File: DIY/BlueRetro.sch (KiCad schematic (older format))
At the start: 22 parts, among them J2 Conn_01x19, J3 Conn_01x19, P1 DC Ctrl slot, P1 GC Ctrl slot, P1 N64 Ctrl slot, P2 DC Ctrl slot, P2 GC Ctrl slot, P2 N64 Ctrl slot, P3 DC Ctrl slot, P3 GC Ctrl slot, P3 N64 Ctrl slot, P4 DC Ctrl slot, P4 GC Ctrl slot, P4 N64 Ctrl slot

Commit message: [DIY] Update DIY & cable adapter schematic base on new DB25 mapping
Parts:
- removed J?: DB25_Female, symbol Connector:DB25_Female
- removed J? (x3): DB25_Male, symbol Connector:DB25_Male
- removed JP1, JP2: Conn_02x14_Odd_Even, symbol Connector_Generic:Conn_02x14_Odd_Even
- removed P1, P2, P3, P4: N64 Ctrl slot, symbol Connector_Generic:Conn_01x03
- removed P1, P2, P3, P4: DC Ctrl slot, symbol Connector_Generic_Shielded:Conn_01x05_Shielded
- removed P1, P2, P3, P4: GC Ctrl slot, symbol Connector_Generic_Shielded:Conn_01x06_Shielded
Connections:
- wire segments 342 -> 81
- no-connect marks 78 -> 10
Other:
- note removed: "* Always use external power for this board.\n If using N64 make sure to unplug 3.3v from DB25.\n** Remove R11, R23, R134, R136, R136, R137, R138, R139, R164 & R168\n** Short R12 & R24\n*** Don't short TXD and RXD0"
- note removed: "Dreamcast cable"
- note removed: "ESP-WROVER-KIT V4.1 (PHASE OUT, NOT RECOMMENDED)"
- note removed: "GameCube cable"
- note removed: "N64 cable"
- moved on the sheet: J2, J3

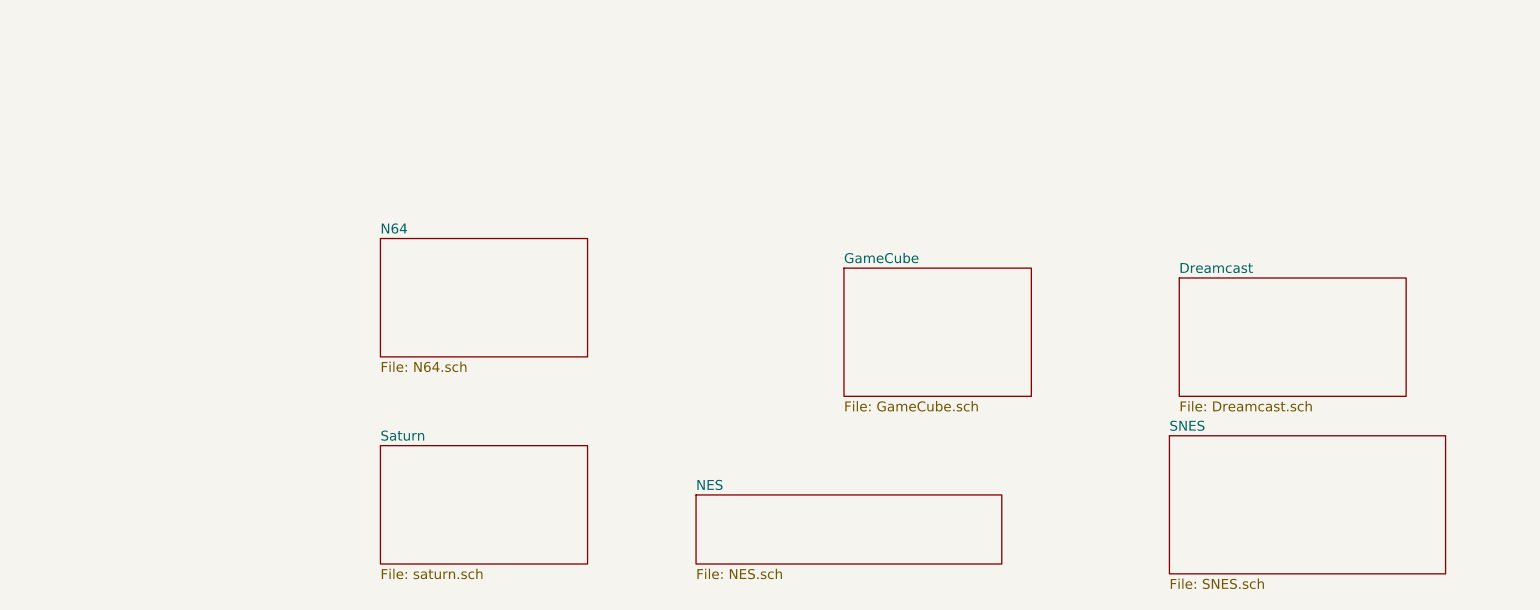
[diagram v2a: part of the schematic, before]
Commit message: Update adapter cable schematics
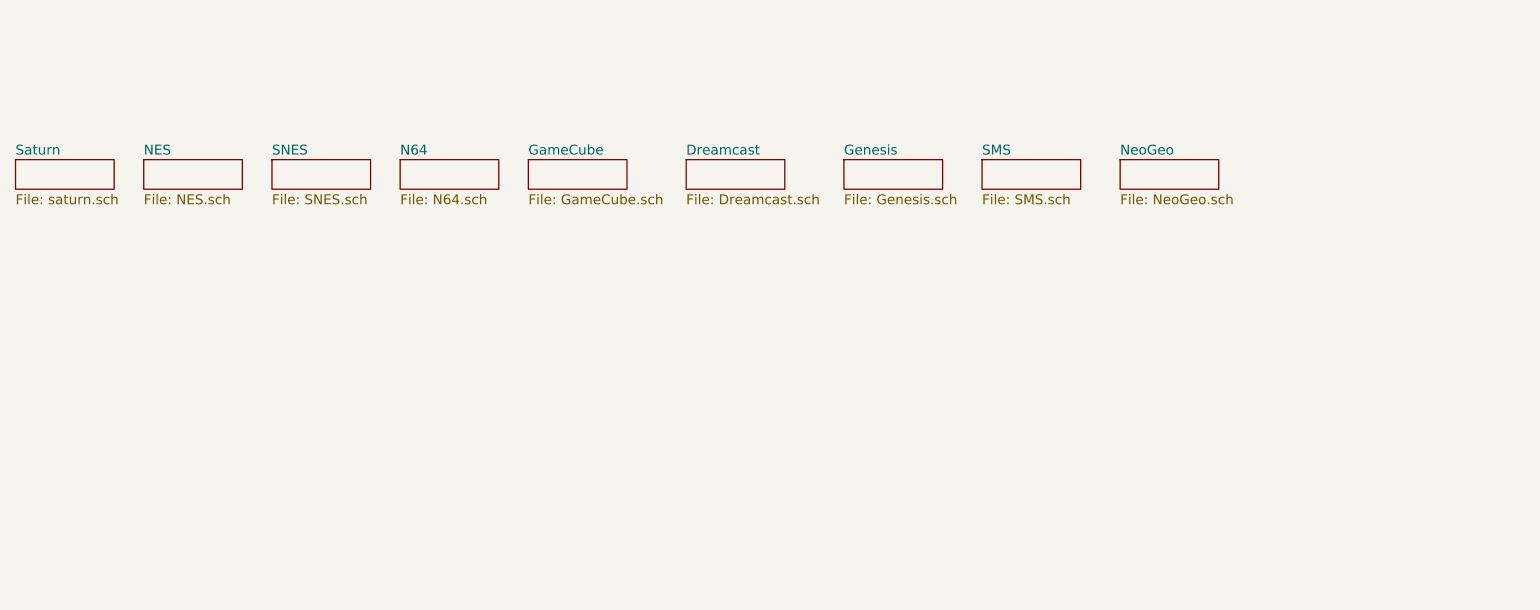
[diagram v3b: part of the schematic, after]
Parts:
- gave numbers to parts that had none: 2
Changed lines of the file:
@@
 $Descr USLetter 11000 8500
 encoding utf-8
-Sheet 1 7
+Sheet 1 10
 Title "BlueRetro DIY"
 Date "2020-10-02"
@@
 ESP32-DevKitC V4 w/ WROOM
 $Comp
-L Connector:DB25_Female J?
+L Connector:DB25_Female J6
 U 1 1 5ECD4943
 P 7600 4150
-F 0 "J?" H 7780 4196 50  0001 L CNN
+F 0 "J6" H 7780 4196 50  0001 L CNN
 F 1 "DB25_Female" H 7350 5550 50  0000 L CNN
 F 2 "" H 7600 4150 50  0001 C CNN
@@
 I35
 $Comp
-L power:GND #PWR?
+L power:GND #PWR010
 U 1 1 5ECD4975
 P 6800 4650
-F 0 "#PWR?" H 6800 4400 50  0001 C CNN
+F 0 "#PWR010" H 6800 4400 50  0001 C CNN
 F 1 "GND" H 6805 4477 50  0000 C CNN
 F 2 "" H 6800 4650 50  0001 C CNN
@@
 	6800 4550 6800 4650
 $Comp
-L power:+3V3 #PWR?
+L power:+3V3 #PWR09
 U 1 1 5ECD4984
 P 6600 3900
-F 0 "#PWR?" H 6600 3750 50  0001 C CNN
+F 0 "#PWR09" H 6600 3750 50  0001 C CNN
 F 1 "+3V3" H 6615 4073 50  0000 C CNN
 F 2 "" H 6600 3900 50  0001 C CNN
@@
 NoConn ~ 7300 4350
 $Comp
-L power:+5V #PWR?
+L power:+5V #PWR08
 U 1 1 5ECD4991
 P 6450 4100
-F 0 "#PWR?" H 6450 3950 50  0001 C CNN
+F 0 "#PWR08" H 6450 3950 50  0001 C CNN
 F 1 "+5V" H 6465 4273 50  0000 C CNN
 F 2 "" H 6450 4100 50  0001 C CNN
@@
 	3400 3750 3200 3750
 $Comp
-L Connector_Generic:Conn_02x06_Top_Bottom J?
+L Connector_Generic:Conn_02x06_Top_Bottom J5
 U 1 1 5EC73236
 P 3700 3850
-F 0 "J?" H 3750 4267 50  0001 C CNN
+F 0 "J5" H 3750 4267 50  0001 C CNN
 F 1 "PmodMicroSD" H 3750 4175 50  0000 C CNN
 F 2 "" H 3700 3850 50  0001 C CNN
@@
 IO27
 $Comp
-L power:+5V #PWR?
+L power:+5V #PWR05
 U 1 1 5F0C98F7
 P 4400 4850
-F 0 "#PWR?" H 4400 4700 50  0001 C CNN
+F 0 "#PWR05" H 4400 4700 50  0001 C CNN
 F 1 "+5V" H 4400 5000 50  0000 C CNN
 F 2 "" H 4400 4850 50  0001 C CNN
@@
 	4400 4900 4900 4900
 $Comp
-L power:+3V3 #PWR?
+L power:+3V3 #PWR06
 U 1 1 5F0D5356
 P 4450 3050
-F 0 "#PWR?" H 4450 2900 50  0001 C CNN
+F 0 "#PWR06" H 4450 2900 50  0001 C CNN
 F 1 "+3V3" H 4465 3223 50  0000 C CNN
 F 2 "" H 4450 3050 50  0001 C CNN
@@
 	4450 3100 4900 3100
 $Comp
-L power:GND #PWR?
+L power:GND #PWR02
 U 1 1 5F0ECEA2
 P 3650 4300
-F 0 "#PWR?" H 3650 4050 50  0001 C CNN
+F 0 "#PWR02" H 3650 4050 50  0001 C CNN
 F 1 "GND" H 3655 4127 50  0000 C CNN
 F 2 "" H 3650 4300 50  0001 C CNN
@@
 	3900 4050 4000 4050
 $Comp
-L power:+3V3 #PWR?
+L power:+3V3 #PWR01
 U 1 1 5F1056D7
 P 3050 4100
-F 0 "#PWR?" H 3050 3950 50  0001 C CNN
+F 0 "#PWR01" H 3050 3950 50  0001 C CNN
 F 1 "+3V3" H 3065 4273 50  0000 C CNN
 F 2 "" H 3050 4100 50  0001 C CNN
@@
 	3050 4150 3050 4100
 $Comp
-L power:+3V3 #PWR?
+L power:+3V3 #PWR03
 U 1 1 5F146FA2
 P 4250 4100
-F 0 "#PWR?" H 4250 3950 50  0001 C CNN
+F 0 "#PWR03" H 4250 3950 50  0001 C CNN
 F 1 "+3V3" H 4265 4273 50  0000 C CNN
 F 2 "" H 4250 4100 50  0001 C CNN
@@
 	4250 4150 4250 4100
 $Comp
-L power:GND #PWR?
+L power:GND #PWR04
 U 1 1 5F15536E
 P 4400 4450
-F 0 "#PWR?" H 4400 4200 50  0001 C CNN
+F 0 "#PWR04" H 4400 4200 50  0001 C CNN
 F 1 "GND" H 4405 4277 50  0000 C CNN
 F 2 "" H 4400 4450 50  0001 C CNN
@@
 	5550 4400 5750 4400
 $Comp
-L power:GND #PWR?
+L power:GND #PWR07
 U 1 1 5F19D657
 P 6000 3800
-F 0 "#PWR?" H 6000 3550 50  0001 C CNN
+F 0 "#PWR07" H 6000 3550 50  0001 C CNN
 F 1 "GND" H 6005 3627 50  0000 C CNN
 F 2 "" H 6000 3800 50  0001 C CNN
@@
 NoConn ~ 5550 4900
 $Sheet
-S 2200 10150 1050 600
+S 350  8700 500  150
 U 5F127084
 F0 "Saturn" 50
@@
 $EndSheet
 $Sheet
-S 3800 10400 1550 350
+S 1000 8700 500  150
 U 5F1E85DD
 F0 "NES" 50
@@
 $EndSheet
 $Sheet
-S 6200 10100 1400 700
+S 1650 8700 500  150
 U 5F2C5C0D
 F0 "SNES" 50
@@
 $EndSheet
 $Sheet
-S 2200 9100 1050 600
+S 2300 8700 500  150
 U 5F457716
 F0 "N64" 50
@@
 $EndSheet
 $Sheet
-S 4550 9250 950  650
+S 2950 8700 500  150
 U 5F457D26
 F0 "GameCube" 50
@@
 $EndSheet
 $Sheet
-S 6250 9300 1150 600
+S 3750 8700 500  150
 U 5F458329
 F0 "Dreamcast" 50
 F1 "Dreamcast.sch" 50
 $EndSheet
+$Sheet
+S 4550 8700 500  150
+U 5F9FC91E
+F0 "Genesis" 50
+F1 "Genesis.sch" 50
+$EndSheet
+$Sheet
+S 5250 8700 500  150
+U 5FD29386
+F0 "SMS" 50
+F1 "SMS.sch" 50
+$EndSheet
+$Sheet
+S 5950 8700 500  150
+U 5FD296AA
+F0 "NeoGeo" 50
+F1 "NeoGeo.sch" 50
+$EndSheet
 $EndSCHEMATC
